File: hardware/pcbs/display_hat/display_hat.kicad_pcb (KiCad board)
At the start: 2 copper layers, 31 x 65 mm, 5 parts, among them J1 Conn_02x20_Odd_Even

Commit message: hat_pcbs are almost done
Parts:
- added C1: 1μF, Capacitor_SMD:C_0805_2012Metric, B.Cu at (3.81, 31.1)
- added J2: Header_01x08, Connector_MTA-100:mta100_01x8_P2.54_640455-8, F.Cu at (-1.29, 34.0)
- added J3: Header_01x08, Connector_MTA-100:mta100_01x8_P2.54_640455-8, F.Cu at (-1.29, 56.5)
- added J4: MTA100_02, Connector_MTA-100:mta100_01x2_P2.54_640455-2, F.Cu at (-1.29, 11.4)
- added JP1: PWR FROM SIDE, Connector_PinHeader_2.54mm:PinHeader_1x02_P2.54mm_Vertical, F.Cu at (-5.08, 4.45)
- added JP2: PWR FROM MAIN, Connector_PinHeader_2.54mm:PinHeader_1x02_P2.54mm_Vertical, F.Cu at (-5.08, 63.2)
- added R1: 10kΩ, Resistor_SMD:R_0805_2012Metric, B.Cu at (1.91, 41.3)
- J1: value Conn_02x20_Odd_Even -> WAVESHARE_HAT_HEADER
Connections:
- J1 pad 1: unconnected-(J1-Pin_1-Pad1) -> +3.3V
- J1 pad 12: unconnected-(J1-Pin_12-Pad12) -> /MAIN_CS
- J1 pad 13: unconnected-(J1-Pin_13-Pad13) -> /MAIN_RST
- J1 pad 14: unconnected-(J1-Pin_14-Pad14) -> GND
- J1 pad 15: unconnected-(J1-Pin_15-Pad15) -> /MAIN_DC
- J1 pad 16: unconnected-(J1-Pin_16-Pad16) -> /SIDE_RST
- J1 pad 17: unconnected-(J1-Pin_17-Pad17) -> +3.3V
- J1 pad 18: unconnected-(J1-Pin_18-Pad18) -> /SIDE_RST
- J1 pad 19: unconnected-(J1-Pin_19-Pad19) -> /SIDE_DAT
- J1 pad 2: unconnected-(J1-Pin_2-Pad2) -> /+5V
- J1 pad 20: unconnected-(J1-Pin_20-Pad20) -> GND
- J1 pad 23: unconnected-(J1-Pin_23-Pad23) -> /SIDE_CLK
- J1 pad 24: unconnected-(J1-Pin_24-Pad24) -> /SIDE_CS_L
- J1 pad 25: unconnected-(J1-Pin_25-Pad25) -> GND
- J1 pad 26: unconnected-(J1-Pin_26-Pad26) -> /SIDE_CS_R
- J1 pad 29: unconnected-(J1-Pin_29-Pad29) -> /SIDE_DC
- J1 pad 30: unconnected-(J1-Pin_30-Pad30) -> GND
- J1 pad 32: unconnected-(J1-Pin_32-Pad32) -> /BL
- J1 pad 33: unconnected-(J1-Pin_33-Pad33) -> /BL
- J1 pad 34: unconnected-(J1-Pin_34-Pad34) -> GND
- J1 pad 35: unconnected-(J1-Pin_35-Pad35) -> /BL
- J1 pad 38: unconnected-(J1-Pin_38-Pad38) -> /MAIN_DAT
- J1 pad 39: unconnected-(J1-Pin_39-Pad39) -> GND
- J1 pad 4: unconnected-(J1-Pin_4-Pad4) -> /+5V
- J1 pad 40: unconnected-(J1-Pin_40-Pad40) -> /MAIN_CLK
- J1 pad 6: unconnected-(J1-Pin_6-Pad6) -> GND
- J1 pad 7: unconnected-(J1-Pin_7-Pad7) -> /SIDE_DC
- J1 pad 9: unconnected-(J1-Pin_9-Pad9) -> GND
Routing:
- net +3.3V: track 0.00 -> 107.2 mm, vias 0 -> 2
- net /SIDE_DC: track 0.00 -> 48.4 mm
- net /MAIN_CS: track 0.00 -> 47.4 mm
- net Net-(J2-Pin_8): track 0.00 -> 36.5 mm
- net /MAIN_DC: track 0.00 -> 28.9 mm, vias 0 -> 2
- net /MAIN_RST: track 0.00 -> 28.6 mm
- net /SIDE_CS_L: track 0.00 -> 25.2 mm
- net /SIDE_RST: track 0.00 -> 22.5 mm
- net /SIDE_CS_R: track 0.00 -> 22.3 mm
- net /BL: track 0.00 -> 22.1 mm
- net /MAIN_DAT: track 0.00 -> 19.9 mm
- net /MAIN_CLK: track 0.00 -> 19.2 mm
- net /SIDE_CLK: track 0.00 -> 16.2 mm
- net Net-(J3-Pin_7): track 0.00 -> 14.8 mm
- net /SIDE_DAT: track 0.00 -> 9.12 mm
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- added copper zone on B.Cu, net GND
- added copper zone on F.Cu, net GND
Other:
- outline, holes or cut-outs redrawn

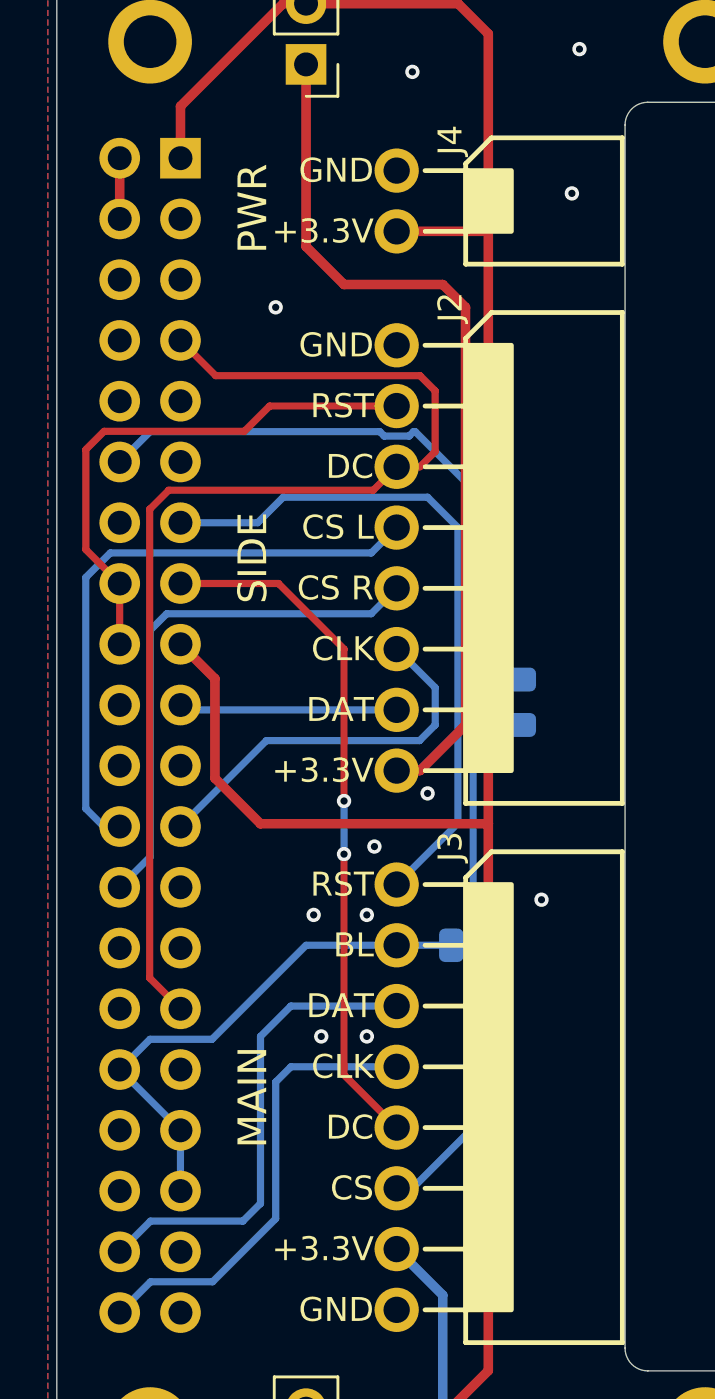
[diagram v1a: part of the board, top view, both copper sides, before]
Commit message: hat_pcbs: add some resistors
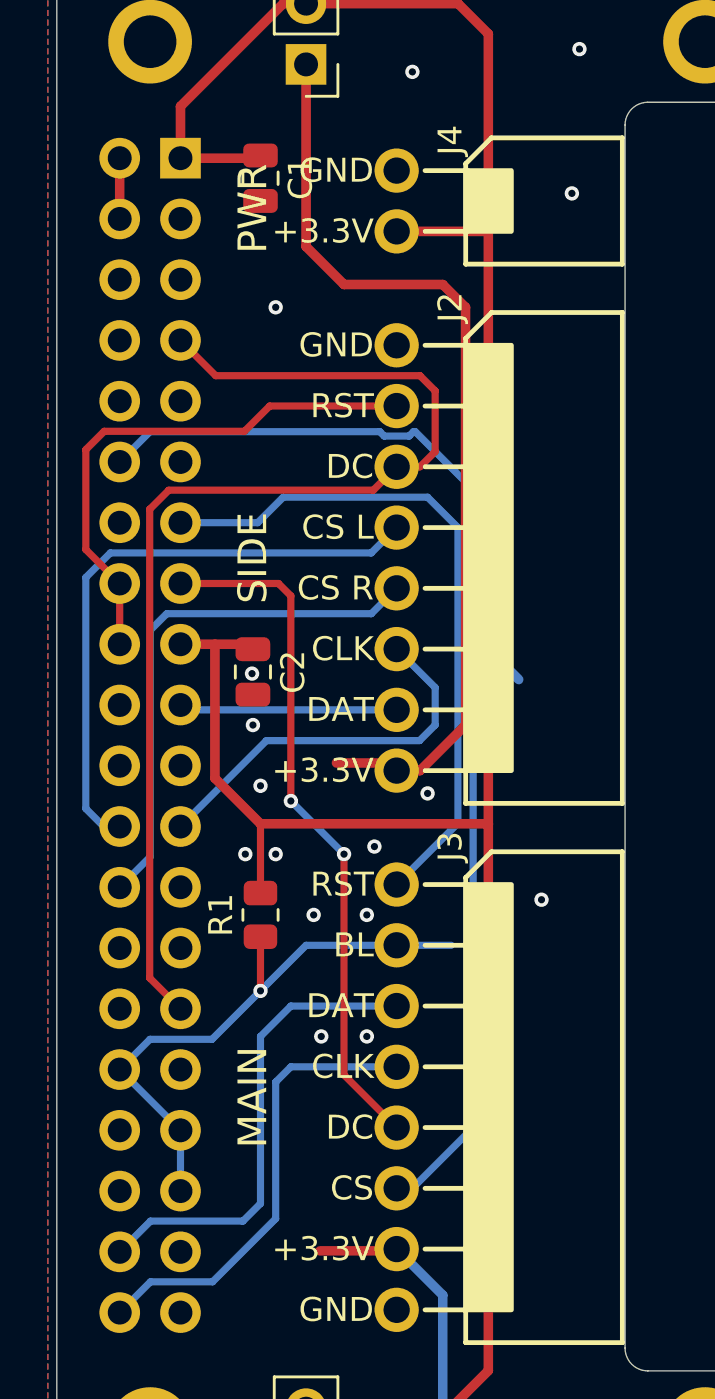
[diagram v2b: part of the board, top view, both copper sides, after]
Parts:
- added C2: 1μF, Capacitor_SMD:C_0805_2012Metric, F.Cu at (-7.30, 29.8)
- C1, R1: moved to F.Cu
- moved C1 24.4 mm to (-6.99, 9.21)
- moved R1 8.98 mm to (-6.99, 40.0), turned to 90 degrees
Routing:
- net +3.3V: track 107.2 -> 116.1 mm
- net Net-(J3-Pin_7): track 14.8 -> 18.0 mm
- net Net-(J2-Pin_8): track 36.5 -> 39.1 mm
- net /BL: track 22.1 -> 24.4 mm, vias 0 -> 1
- net GND: vias 11 -> 16

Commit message: hat_pcbs: cosmetic fixes
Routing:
- net +3.3V: track 116.1 -> 111.2 mm, vias 2 -> 0
- net Net-(J3-Pin_7): track 18.0 -> 14.9 mm
- net /BL: track 24.4 -> 22.1 mm
- net Net-(J2-Pin_8): track 39.1 -> 36.9 mm
- net /MAIN_RST: track 28.6 -> 29.1 mm
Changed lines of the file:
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@@
 		(tags "MTA-100 2.54mm header single row polarized")
 		(property "Reference" "J4"
-			(at 3.175 2.245 90)
+			(at 3.237894 2.618911 90)
 			(layer "F.SilkS")
 			(effects
@@
 		)
 		(fp_text user "${Purpose}"
-			(at 0.9525 -6.01 90)
+			(at 5.3975 0.34 180)
 			(layer "F.SilkS")
 			(effects
@@
 		(tags "capacitor")
 		(property "Reference" "C1"
-			(at 0 -1.68 90)
+			(at -2.54 1.5875 180)
 			(layer "F.SilkS")
 			(effects
@@
 	)
 	(segment
-		(start 0.9925 41.275)
-		(end -1.2925 41.275)
-		(width 0.3)
-		(layer "B.Cu")
-		(net 9)
-	)
-	(segment
 		(start -12.87 46.47)
 		(end -10.33 49.01)
@@
 	)
 	(segment
-		(start 1.27 23.8125)
+		(start 1.905 24.4475)
 		(end 0 22.5425)
 		(width 0.3)
@@
 	)
 	(segment
-		(start -1.2925 38.735)
-		(end 1.27 36.1725)
+		(start 1.905 35.5375)
+		(end 1.905 24.4475)
 		(width 0.3)
 		(layer "B.Cu")
@@
 	)
 	(segment
-		(start 0 22.5425)
-		(end -6.0325 22.5425)
+		(start -7.1 23.61)
+		(end -10.33 23.61)
 		(width 0.3)
 		(layer "B.Cu")
@@
 	)
 	(segment
-		(start -7.1 23.61)
-		(end -10.33 23.61)
+		(start 0 22.5425)
+		(end -6.0325 22.5425)
 		(width 0.3)
 		(layer "B.Cu")
@@
 	)
 	(segment
-		(start 1.27 36.1725)
-		(end 1.27 23.8125)
+		(start -6.0325 22.5425)
+		(end -7.1 23.61)
 		(width 0.3)
 		(layer "B.Cu")
@@
 	)
 	(segment
-		(start -6.0325 22.5425)
-		(end -7.1 23.61)
+		(start -1.2925 38.735)
+		(end 1.905 35.5375)
 		(width 0.3)
 		(layer "B.Cu")
@@
 	)
 	(segment
-		(start -1.812339 19.9875)
-		(end -1.99719 19.802649)
-		(width 0.3)
-		(layer "B.Cu")
-		(net 19)
-	)
-	(segment
-		(start -1.99719 19.802649)
-		(end -11.602649 19.802649)
+		(start -1.2925 51.435)
+		(end -0.635 51.435)
 		(width 0.3)
 		(layer "B.Cu")
@@
 	)
 	(segment
-		(start -0.772661 19.9875)
-		(end -1.812339 19.9875)
+		(start -0.635 51.435)
+		(end 2.54 48.26)
 		(width 0.3)
 		(layer "B.Cu")
@@
 	)
 	(segment
-		(start -0.517352 19.802649)
-		(end -0.58781 19.802649)
+		(start -0.332501 19.9875)
+		(end -5.7 19.9875)
 		(width 0.3)
 		(layer "B.Cu")
@@
 	)
 	(segment
-		(start 1.905 48.895)
-		(end 1.905 22.225001)
+		(start 2.54 22.860001)
+		(end -0.332501 19.9875)
 		(width 0.3)
 		(layer "B.Cu")
@@
 	)
 	(segment
-		(start 1.905 22.225001)
-		(end -0.517352 19.802649)
+		(start -11.596445 19.796445)
+		(end -12.87 21.07)
 		(width 0.3)
 		(layer "B.Cu")
@@
 	)
 	(segment
-		(start -11.602649 19.802649)
-		(end -12.87 21.07)
+		(start -5.715 20.0025)
+		(end -5.921055 19.796445)
 		(width 0.3)
 		(layer "B.Cu")
@@
 	)
 	(segment
-		(start -1.2925 51.435)
-		(end -0.635 51.435)
+		(start -5.921055 19.796445)
+		(end -11.596445 19.796445)
 		(width 0.3)
 		(layer "B.Cu")
@@
 	)
 	(segment
-		(start -0.635 51.435)
-		(end 1.905 48.895)
+		(start -5.7 19.9875)
+		(end -5.715 20.0025)
 		(width 0.3)
 		(layer "B.Cu")
@@
 	)
 	(segment
-		(start -0.58781 19.802649)
-		(end -0.772661 19.9875)
+		(start 2.54 48.26)
+		(end 2.54 22.860001)
 		(width 0.3)
 		(layer "B.Cu")
@@
 	)
 	(segment
-		(start -3.81 33.6525)
-		(end -1.6125 33.6525)
-		(width 0.4)
-		(layer "F.Cu")
-		(net 26)
-	)
-	(segment
 		(start 1.5875 14.605)
 		(end 0.635 13.6525)
@@
 	)
 	(segment
-		(start -4.5 54.05)
-		(end -1.3675 54.05)
-		(width 0.4)
-		(layer "F.Cu")
-		(net 27)
-	)
-	(segment
 		(start -1.3675 54.05)
 		(end -1.2925 53.975)
@@
 	)
 	(segment
+		(start -5.08 1.91)
+		(end -5.085 1.905)
+		(width 0.4)
+		(layer "F.Cu")
+		(net 29)
+	)
+	(segment
 		(start -1.2925 11.43)
 		(end 2.54 11.43)
@@
 	)
 	(segment
-		(start -8.89 28.69)
-		(end -8.89 34.29)
-		(width 0.4)
-		(layer "F.Cu")
-		(net 29)
-	)
-	(segment
-		(start -6.0375 1.91)
-		(end -5.08 1.91)
+		(start -5.085 1.905)
+		(end -6.35 1.905)
 		(width 0.4)
 		(layer "F.Cu")
@@
 	)
 	(segment
-		(start -10.33 6.2025)
-		(end -6.0375 1.91)
+		(start -8.89 28.69)
+		(end -8.89 34.29)
 		(width 0.4)
 		(layer "F.Cu")
@@
 	)
 	(segment
+		(start -6.35 1.905)
+		(end -6.985 2.54)
+		(width 0.4)
+		(layer "F.Cu")
+		(net 29)
+	)
+	(segment
 		(start 0.3125 60.6475)
 		(end -5.08 60.6475)
@@
 	)
 	(segment
-		(start -10.33 8.37)
-		(end -10.33 6.2025)
+		(start 0.3175 60.6425)
+		(end 0.3125 60.6475)
 		(width 0.4)
 		(layer "F.Cu")
@@
 	)
 	(segment
-		(start 0.3175 60.6425)
-		(end 0.3125 60.6475)
+		(start -6.985 2.54)
+		(end -6.985 8.2575)
 		(width 0.4)
 		(layer "F.Cu")
@@
 		(net 29)
 	)
-	(via
-		(at 2.54 28.575)
-		(size 0.6)
-		(drill 0.3)
-		(layers "F.Cu" "B.Cu")
-		(net 29)
-	)
-	(via
-		(at 2.54 40.005)
-		(size 0.6)
-		(drill 0.3)
-		(layers "F.Cu" "B.Cu")
-		(net 29)
-	)
-	(segment
-		(start 2.8175 40.2825)
-		(end 2.54 40.005)
-		(width 0.3)
-		(layer "B.Cu")
-		(net 29)
-	)
-	(segment
-		(start 3.81 30.165)
-		(end 2.54 28.895)
-		(width 0.4)
-		(layer "B.Cu")
-		(net 29)
-	)
-	(segment
-		(start 2.8175 41.275)
-		(end 2.8175 40.2825)
-		(width 0.3)
-		(layer "B.Cu")
-		(net 29)
-	)
-	(segment
-		(start 2.54 28.895)
-		(end 2.54 28.575)
-		(width 0.4)
-		(layer "B.Cu")
-		(net 29)
-	)

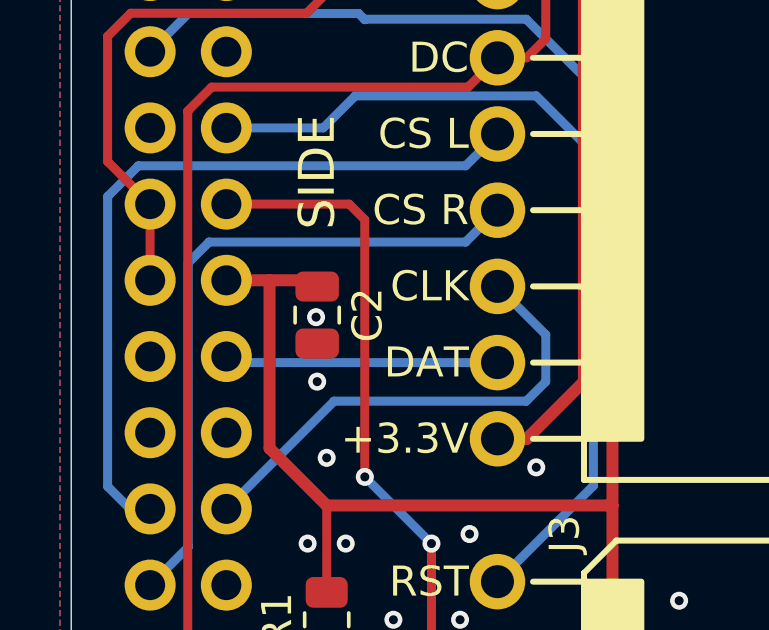
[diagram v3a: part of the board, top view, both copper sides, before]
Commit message: power_board: BIGGER inductors
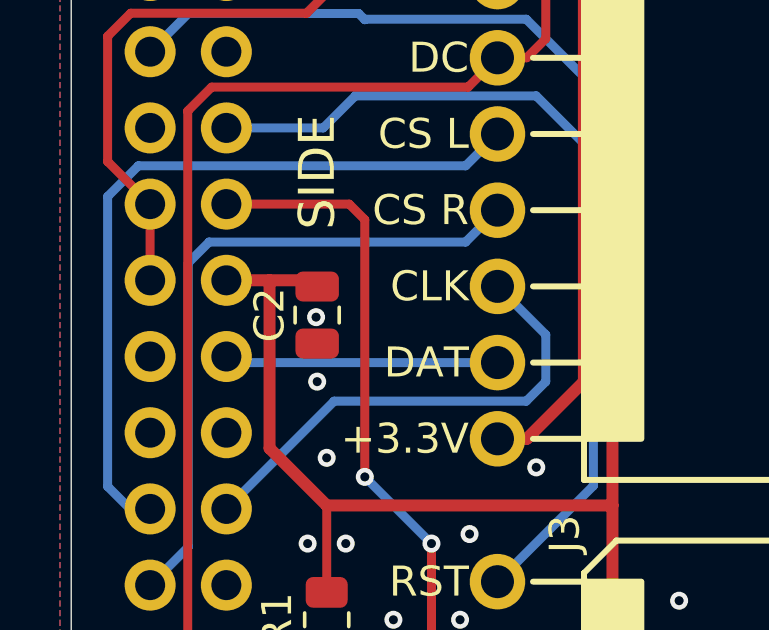
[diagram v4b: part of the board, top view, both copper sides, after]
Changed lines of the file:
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@@
 		(tags "capacitor")
 		(property "Reference" "C2"
-			(at 0 -1.68 90)
+			(at -0.0025 1.5875 90)
 			(layer "F.SilkS")
 			(effects

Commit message: hat_pcbs: final changes
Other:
- board text added: "FOSDEM display hat rev. A"
- board text added: "JLCJLCJLCJLC"
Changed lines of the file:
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@@
 	)
 	(paper "A4")
+	(title_block
+		(comment 4 "AISLER Project ID: VFRMODMF")
+	)
 	(layers
 		(0 "F.Cu" signal)
@@
 		(layer "Edge.Cuts")
 	)
+	(gr_text "JLCJLCJLCJLC"
+		(at 5.08 21.59 90)
+		(layer "B.SilkS")
+		(effects
+			(font
+				(size 1 1)
+				(thickness 0.1)
+			)
+			(justify left bottom mirror)
+		)
+	)
+	(gr_text "FOSDEM display hat rev. A"
+		(at 6.8975 21.305 90)
+		(layer "B.SilkS")
+		(effects
+			(font
+				(size 1 1)
+				(thickness 0.1)
+			)
+			(justify left bottom mirror)
+		)
+	)
 	(segment
